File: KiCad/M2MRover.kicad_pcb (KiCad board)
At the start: 2 copper layers, 80 x 90 mm, 58 parts, among them J1 microbit_edge_connector, J10 Ultrasonic Forward, J2 Left Motor, J3 Right Motor, J4 Serial (Bluetooth), J5 MPU6050 Gyro & Acc GY-521, J6 Compass GY-273, J7 Light Detection, J8 Servo, J9 Ultrasonic Down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

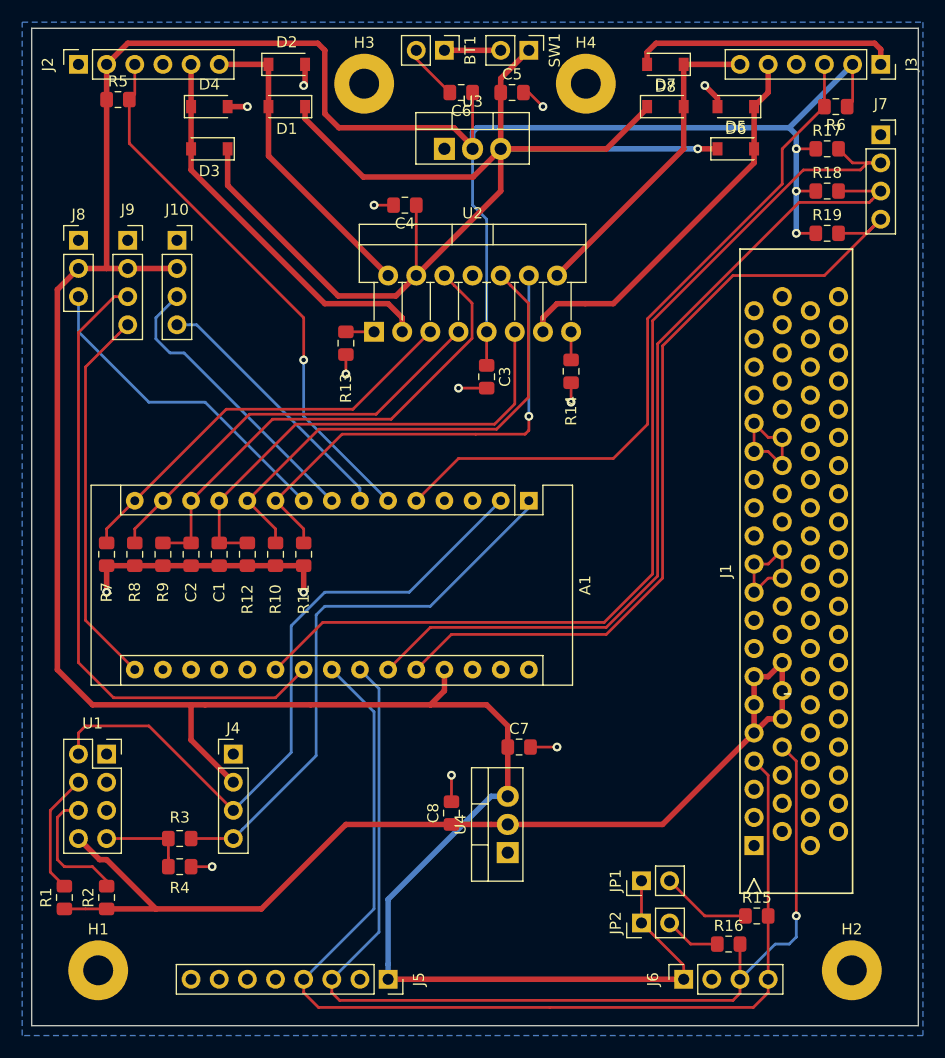
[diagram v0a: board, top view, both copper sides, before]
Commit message: Track all remaining of components
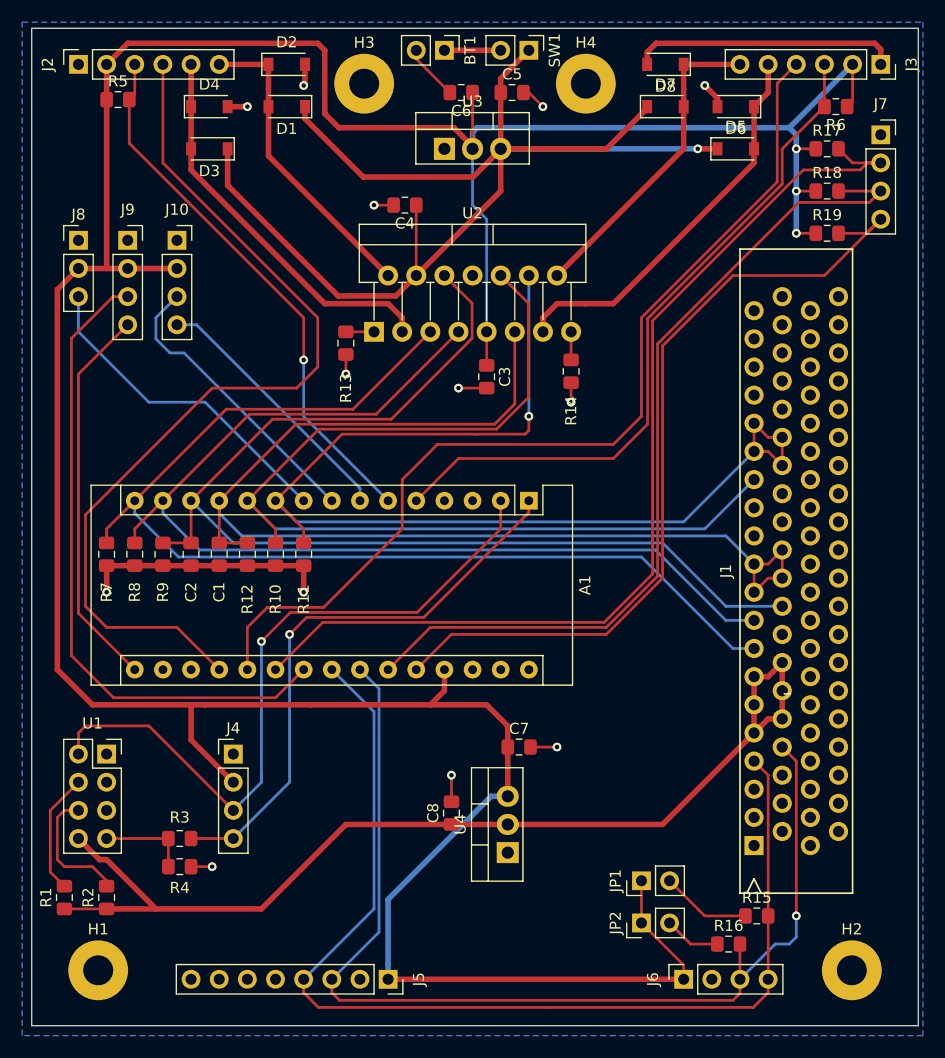
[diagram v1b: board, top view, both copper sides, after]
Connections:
- J1 pad 29: IN3 -> IN1
- J1 pad 33: IN1 -> IN2
- J1 pad 35: IN2 -> ENA
- J1 pad 53: IN4 -> IN3
- J1 pad 55: ENA -> IN4
- J1 pad 57: ENA -> IN4
- J1 pad 59: ENA -> IN4
- J1 pad 61: ENA -> IN4
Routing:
- net Right_LED: track 0.00 -> 87.4 mm
- net Left_LED: track 0.00 -> 82.3 mm
- net IN1: track 37.8 -> 99.9 mm
- net IN2: track 37.8 -> 96.3 mm
- net IN4: track 44.3 -> 102.1 mm
- net ENB: track 54.4 -> 105.6 mm
- net IN3: track 46.1 -> 94.7 mm
- net ENA: track 55.7 -> 101.8 mm
- net RX: track 61.7 -> 63.9 mm, vias 0 -> 1
- net TX: track 50.9 -> 51.5 mm, vias 0 -> 1
- net Ultrasonic_Down_Echo: track 58.3 -> 58.8 mm
- net Ultrasonic_Down_Trigger: track 34.5 -> 35.1 mm

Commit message: Add power plain on front side copper
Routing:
- net GND: vias 13 -> 27
- added copper zone on F.Cu, net GND
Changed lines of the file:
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@@
     (thickness 1.6)
     (drawings 10)
-    (tracks 401)
+    (tracks 415)
     (zones 0)
     (modules 58)
@@
     (via_min_size 0.4)
     (via_min_drill 0.3)
+    (user_via 1.6 0.8)
     (uvia_size 0.3)
     (uvia_drill 0.1)
@@
   (via (at 152.4 109.855) (size 0.8) (drill 0.4) (layers F.Cu B.Cu) (net 1))
   (segment (start 150.005 109.855) (end 152.4 109.855) (width 0.25) (layer F.Cu) (net 1))
+  (via (at 165.1 78.74) (size 1.6) (drill 0.8) (layers F.Cu B.Cu) (net 1))
+  (via (at 159.385 105.41) (size 1.6) (drill 0.8) (layers F.Cu B.Cu) (net 1))
+  (via (at 131.445 112.395) (size 1.6) (drill 0.8) (layers F.Cu B.Cu) (net 1))
+  (via (at 150.495 124.46) (size 1.6) (drill 0.8) (layers F.Cu B.Cu) (net 1))
+  (via (at 119.38 127.635) (size 1.6) (drill 0.8) (layers F.Cu B.Cu) (net 1))
+  (via (at 116.205 114.3) (size 1.6) (drill 0.8) (layers F.Cu B.Cu) (net 1))
+  (via (at 123.825 70.485) (size 1.6) (drill 0.8) (layers F.Cu B.Cu) (net 1))
+  (via (at 108.585 56.515) (size 1.6) (drill 0.8) (layers F.Cu B.Cu) (net 1))
+  (via (at 180.34 122.555) (size 1.6) (drill 0.8) (layers F.Cu B.Cu) (net 1))
+  (via (at 172.085 65.405) (size 1.6) (drill 0.8) (layers F.Cu B.Cu) (net 1))
+  (via (at 121.285 98.425) (size 1.6) (drill 0.8) (layers F.Cu B.Cu) (net 1))
+  (via (at 151.765 95.885) (size 1.6) (drill 0.8) (layers F.Cu B.Cu) (net 1))
+  (via (at 156.21 86.995) (size 1.6) (drill 0.8) (layers F.Cu B.Cu) (net 1))
+  (via (at 137.795 95.885) (size 1.6) (drill 0.8) (layers F.Cu B.Cu) (net 1))
   (segment (start 113.665 71.755) (end 109.22 76.2) (width 0.25) (layer F.Cu) (net 2))
   (segment (start 109.22 76.2) (end 109.22 97.79) (width 0.25) (layer F.Cu) (net 2))
@@
   (segment (start 149.86 81.28) (end 149.86 80.01) (width 0.25) (layer F.Cu) (net 5))
   (segment (start 149.86 80.01) (end 149.86 67.31) (width 0.25) (layer B.Cu) (net 5))
+  (segment (start 170.18 80.645) (end 170.18 83.185) (width 0.25) (layer F.Cu) (net 5))
+  (segment (start 172.72 81.915) (end 172.72 84.455) (width 0.25) (layer F.Cu) (net 5))
+  (segment (start 171.45 83.185) (end 170.18 83.185) (width 0.25) (layer F.Cu) (net 5))
+  (segment (start 172.72 84.455) (end 171.45 83.185) (width 0.25) (layer F.Cu) (net 5))
+  (segment (start 171.45 81.915) (end 172.72 81.915) (width 0.25) (layer F.Cu) (net 5))
+  (segment (start 170.18 80.645) (end 171.45 81.915) (width 0.25) (layer F.Cu) (net 5))
+  (segment (start 163.83 89.535) (end 170.18 83.185) (width 0.25) (layer B.Cu) (net 5))
+  (segment (start 127 87.63) (end 128.905 89.535) (width 0.25) (layer B.Cu) (net 5))
+  (segment (start 128.905 89.535) (end 163.83 89.535) (width 0.25) (layer B.Cu) (net 5))
   (segment (start 121.92 87.63) (end 121.92 91.44) (width 0.25) (layer F.Cu) (net 6))
   (segment (start 121.92 91.44) (end 124.46 91.44) (width 0.25) (layer F.Cu) (net 6))
@@
   (segment (start 171.45 94.615) (end 172.72 94.615) (width 0.25) (layer F.Cu) (net 6))
   (segment (start 170.18 95.885) (end 171.45 94.615) (width 0.25) (layer F.Cu) (net 6))
+  (segment (start 167.64 90.805) (end 170.18 93.345) (width 0.25) (layer B.Cu) (net 6))
+  (segment (start 123.96363 90.805) (end 167.64 90.805) (width 0.25) (layer B.Cu) (net 6))
+  (segment (start 121.92 87.63) (end 121.92 88.76137) (width 0.25) (layer B.Cu) (net 6))
+  (segment (start 121.92 88.76137) (end 123.96363 90.805) (width 0.25) (layer B.Cu) (net 6))
   (segment (start 119.38 87.63) (end 119.38 91.44) (width 0.25) (layer F.Cu) (net 8))
   (segment (start 116.84 91.44) (end 119.38 91.44) (width 0.25) (layer F.Cu) (net 8))
@@
   (segment (start 126.734981 80.275019) (end 137.437984 80.275018) (width 0.25) (layer F.Cu) (net 8))
   (segment (start 119.38 87.63) (end 126.734981 80.275019) (width 0.25) (layer F.Cu) (net 8))
-  (segment (start 170.18 80.645) (end 170.18 83.185) (width 0.25) (layer F.Cu) (net 5))
-  (segment (start 172.72 81.915) (end 172.72 84.455) (width 0.25) (layer F.Cu) (net 5))
-  (segment (start 171.45 83.185) (end 170.18 83.185) (width 0.25) (layer F.Cu) (net 5))
-  (segment (start 172.72 84.455) (end 171.45 83.185) (width 0.25) (layer F.Cu) (net 5))
-  (segment (start 171.45 81.915) (end 172.72 81.915) (width 0.25) (layer F.Cu) (net 5))
-  (segment (start 170.18 80.645) (end 171.45 81.915) (width 0.25) (layer F.Cu) (net 5))
-  (segment (start 163.83 89.535) (end 170.18 83.185) (width 0.25) (layer B.Cu) (net 5))
-  (segment (start 127 87.63) (end 128.905 89.535) (width 0.25) (layer B.Cu) (net 5))
-  (segment (start 128.905 89.535) (end 163.83 89.535) (width 0.25) (layer B.Cu) (net 5))
-  (segment (start 167.64 90.805) (end 170.18 93.345) (width 0.25) (layer B.Cu) (net 6))
-  (segment (start 123.96363 90.805) (end 167.64 90.805) (width 0.25) (layer B.Cu) (net 6))
-  (segment (start 121.92 87.63) (end 121.92 88.76137) (width 0.25) (layer B.Cu) (net 6))
-  (segment (start 121.92 88.76137) (end 123.96363 90.805) (width 0.25) (layer B.Cu) (net 6))
   (segment (start 167.64 97.155) (end 172.72 97.155) (width 0.25) (layer B.Cu) (net 8))
   (segment (start 161.925 91.44) (end 167.64 97.155) (width 0.25) (layer B.Cu) (net 8))
@@
     (connect_pads (clearance 0.508))
     (min_thickness 0.254)
+    (fill yes (arc_segments 32) (thermal_gap 0.508) (thermal_bridge_width 0.508))
+    (polygon
+      (pts
+        (xy 104.14 44.45) (xy 185.42 44.45) (xy 185.42 135.89) (xy 104.14 135.89)
+      )
+    )
+  )
+  (zone (net 1) (net_name GND) (layer F.Cu) (hatch edge 0.508)
+    (connect_pads (clearance 0.508))
+    (min_thickness 0.254)
